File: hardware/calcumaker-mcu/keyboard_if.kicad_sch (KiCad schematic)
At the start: 1 part, among them J5 TO KEYBOARD

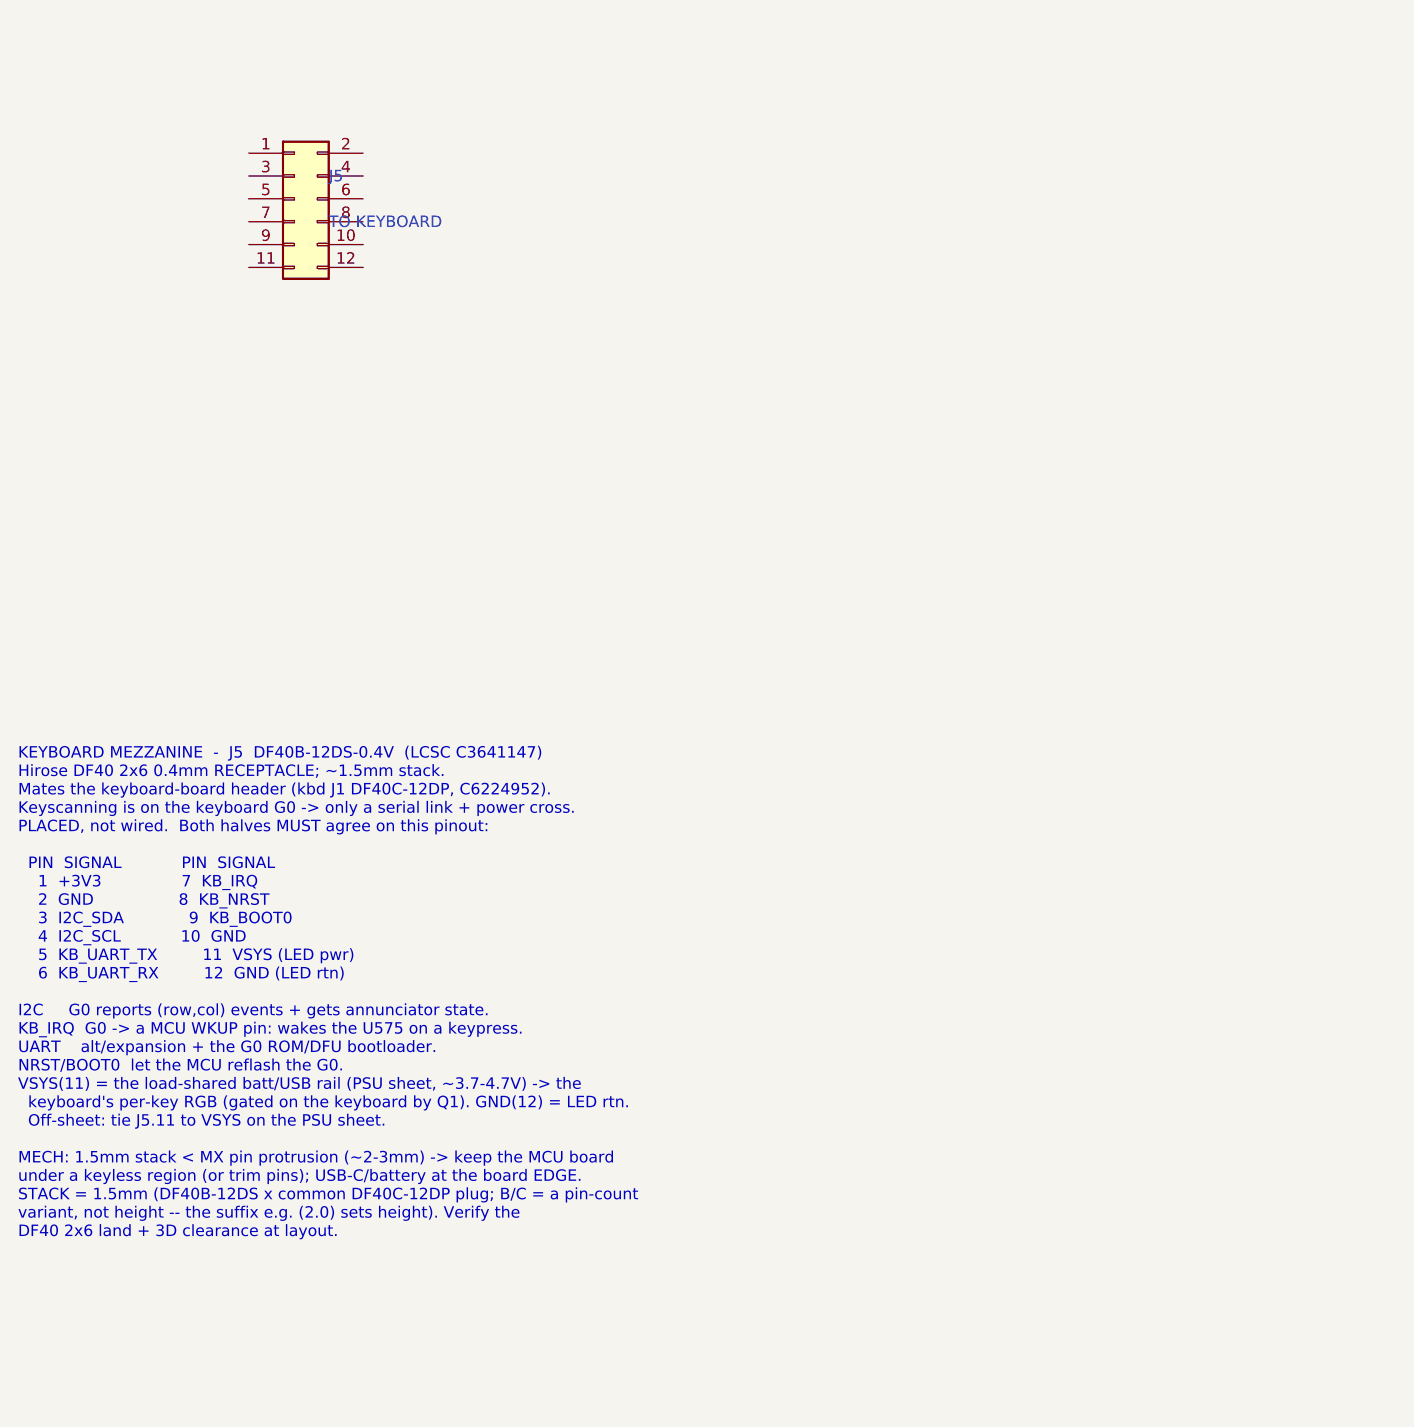
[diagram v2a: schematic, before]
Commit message: hardware: schematic wiring + design/parts updates (WIP)
Pre-existing working-tree changes across the MCU and keyboard boards: wiring
build-out on the mezzanine interfaces (main_if / keyboard_if), MCU/PSU/display/
clock/QSPI sheet edits, per-key row updates, plus DESIGN.md, PARTS.md, and the
two schgen manifests. Committed as-is at the user's request.

Co-Authored-By: Claude Opus 4.8 (1M context) <noreply@anthropic.com>
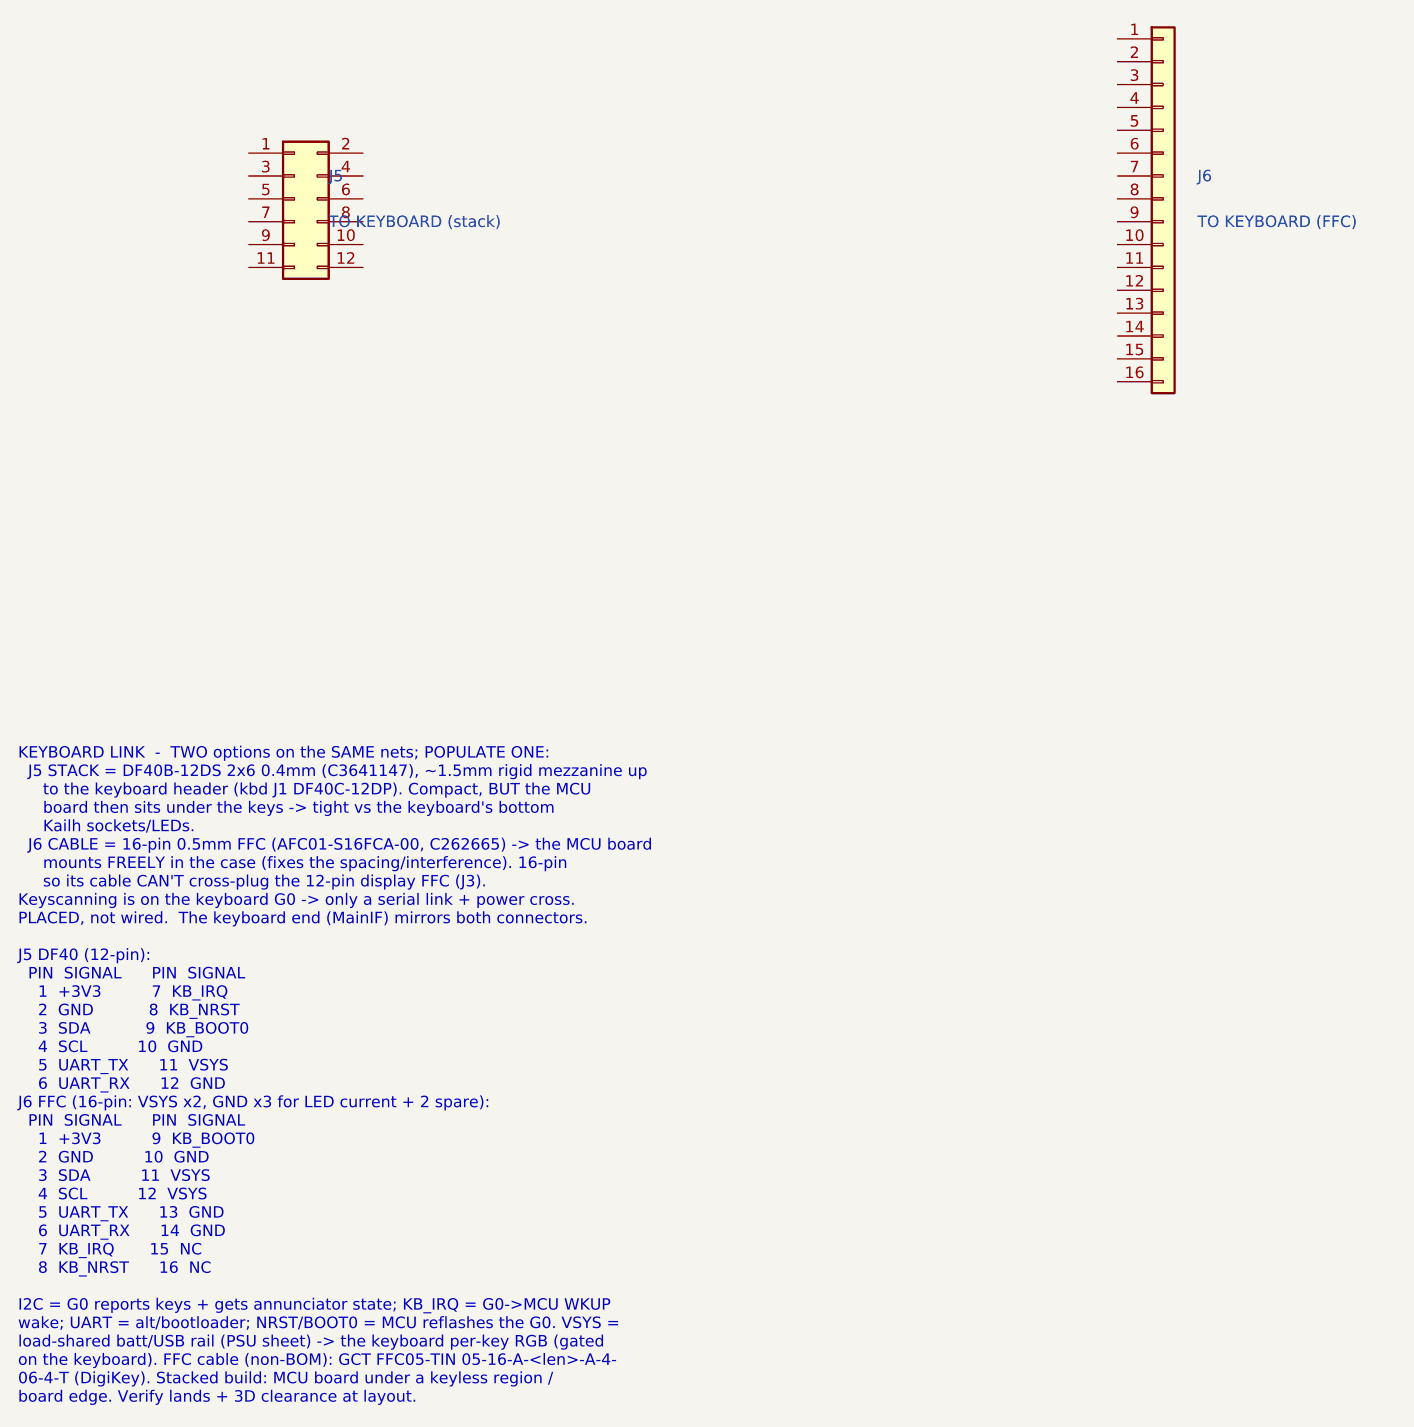
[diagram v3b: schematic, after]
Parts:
- added J6: TO KEYBOARD (FFC), Connector_FFC-FPC:Hirose_FH12-16S-0.5SH_1x16-1MP_P0.50mm_Horizontal, symbol Connector_Generic:Conn_01x16
- J5: value TO KEYBOARD -> TO KEYBOARD (stack)
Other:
- note added: "KEYBOARD LINK - TWO options on the SAME nets; POPULATE ONE: J5 STACK = DF40B-12DS 2x6 0.4mm (C3641147), ~1.5mm rigid mezzanine up to the keyboard header (kbd J1 DF40C-12DP). Compact, BUT the MCU board then sits under the keys -> tight vs the keyboard's bottom Kailh sockets/LEDs. J6 CABLE = 16-pin 0.5mm FFC (AFC01-S16FCA-00, C262665) -> the MCU board mounts FREELY in the case (fixes the spacing/in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"
- note removed: "KEYBOARD MEZZANINE - J5 DF40B-12DS-0.4V (LCSC C3641147) Hirose DF40 2x6 0.4mm RECEPTACLE; ~1.5mm stack. Mates the keyboard-board header (kbd J1 DF40C-12DP, C6224952). Keyscanning is on the keyboard G0 -> only a serial link + power cross. PLACED, not wired. Both halves MUST agree on this pinout: PIN SIGNAL PIN SIGNAL 1 +3V3 7 KB_IRQ 2 GND 8 KB_NRST 3 I2C_SDA 9 KB_BOOT0 4 I2C_SCL 10 GND 5 KB_UART_T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"
- title: Calcumaker 16 — MCU — Keyboard mezzanine (I2C + UART + VSYS to the stacked keyboard) -> Calcumaker 16 — MCU — Keyboard link -- DF40 stack (J5) OR 16-pin FFC cable (J6), populate one
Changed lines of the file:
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@@
 	(paper "A3")
 	(title_block
-		(title "Calcumaker 16 — MCU — Keyboard mezzanine (I2C + UART + VSYS to the stacked keyboard)")
+		(title "Calcumaker 16 — MCU — Keyboard link -- DF40 stack (J5) OR 16-pin FFC cable (J6), populate one")
 		(date "2026-07-06")
 		(rev "0.3")
@@
 			(effects (font (size 1.27 1.27)) (justify left))
 		)
-		(property "Value" "TO KEYBOARD"
+		(property "Value" "TO KEYBOARD (stack)"
 			(at 49.5300 58.4200 0)
 			(effects (font (size 1.27 1.27)) (justify left))
@@
 		)
 	)
-	(text "KEYBOARD MEZZANINE  -  J5  DF40B-12DS-0.4V  (LCSC C3641147)\nHirose DF40 2x6 0.4mm RECEPTACLE; ~1.5mm stack.\nMates the keyboard-board header (kbd J1 DF40C-12DP, C6224952).\nKeyscanning is on the keyboard G0 -> only a serial link + power cross.\nPLACED, not wired.  Both halves MUST agree on this pinout:\n\n  PIN  SIGNAL            PIN  SIGNAL        \n    1  +3V3                7  KB_IRQ        \n    2  GND                 8  KB_NRST       \n    3  I2C_SDA             9  KB_BOOT0      \n    4  I2C_SCL            10  GND           \n    5  KB_UART_TX         11  VSYS (LED pwr)\n    6  KB_UART_RX         12  GND (LED rtn)\n\nI2C     G0 reports (row,col) events + gets annunciator state.\nKB_IRQ  G0 -> a MCU WKUP pin: wakes the U575 on a keypress.\nUART    alt/expansion + the G0 ROM/DFU bootloader.\nNRST/BOOT0  let the MCU reflash the G0.\nVSYS(11) = the load-shared batt/USB rail (PSU sheet, ~3.7-4.7V) -> the\n  keyboard's per-key RGB (gated on the keyboard by Q1). GND(12) = LED rtn.\n  Off-sheet: tie J5.11 to VSYS on the PSU sheet.\n\nMECH: 1.5mm stack < MX pin protrusion (~2-3mm) -> keep the MCU board\nunder a keyless region (or trim pins); USB-C/battery at the board EDGE.\nSTACK = 1.5mm (DF40B-12DS x common DF40C-12DP plug; B/C = a pin-count\nvariant, not height -- the suffix e.g. (2.0) sets height). Verify the\nDF40 2x6 land + 3D clearance at layout."
+	(symbol
+		(lib_id "Connector_Generic:Conn_01x16")
+		(at 142.2400 55.8800 0)
+		(unit 1)
+		(exclude_from_sim no)
+		(in_bom yes)
+		(on_board yes)
+		(dnp no)
+		(property "Reference" "J6"
+			(at 146.0500 53.3400 0)
+			(effects (font (size 1.27 1.27)) (justify left))
+		)
+		(property "Value" "TO KEYBOARD (FFC)"
+			(at 146.0500 58.4200 0)
+			(effects (font (size 1.27 1.27)) (justify left))
+		)
+		(property "Footprint" "Connector_FFC-FPC:Hirose_FH12-16S-0.5SH_1x16-1MP_P0.50mm_Horizontal"
+			(at 142.2400 55.8800 0)
+			(effects (font (size 1.27 1.27))) (hide yes)
+		)
+		(property "Datasheet" "~"
+			(at 142.2400 55.8800 0)
+			(effects (font (size 1.27 1.27))) (hide yes)
+		)
+		(property "LCSC" "C262665"
+			(at 142.2400 55.8800 0)
+			(effects (font (size 1.27 1.27))) (hide yes)
+		)
+		(property "MPN" "AFC01-S16FCA-00"
+			(at 142.2400 55.8800 0)
+			(effects (font (size 1.27 1.27))) (hide yes)
+		)
+		(property "Manufacturer" "JUSHUO"
+			(at 142.2400 55.8800 0)
+			(effects (font (size 1.27 1.27))) (hide yes)
+		)
+		(pin "1")
+		(pin "2")
+		(pin "3")
+		(pin "4")
+		(pin "5")
+		(pin "6")
+		(pin "7")
+		(pin "8")
+		(pin "9")
+		(pin "10")
+		(pin "11")
+		(pin "12")
+		(pin "13")
+		(pin "14")
+		(pin "15")
+		(pin "16")
+		(instances
+			(project "calcumaker-mcu"
+				(path "/ca1c0000-0000-4000-8000-00000000ma01/32aa4625-0e65-45ea-b771-87030b782539"
+					(reference "J6")
+					(unit 1)
+				)
+			)
+		)
+	)
+	(text "KEYBOARD LINK  -  TWO options on the SAME nets; POPULATE ONE:\n  J5 STACK = DF40B-12DS 2x6 0.4mm (C3641147), ~1.5mm rigid mezzanine up\n     to the keyboard header (kbd J1 DF40C-12DP). Compact, BUT the MCU\n     board then sits under the keys -> tight vs the keyboard's bottom\n     Kailh sockets/LEDs.\n  J6 CABLE = 16-pin 0.5mm FFC (AFC01-S16FCA-00, C262665) -> the MCU board\n     mounts FREELY in the case (fixes the spacing/interference). 16-pin\n     so its cable CAN'T cross-plug the 12-pin display FFC (J3).\nKeyscanning is on the keyboard G0 -> only a serial link + power cross.\nPLACED, not wired.  The keyboard end (MainIF) mirrors both connectors.\n\nJ5 DF40 (12-pin):\n  PIN  SIGNAL      PIN  SIGNAL  \n    1  +3V3          7  KB_IRQ  \n    2  GND           8  KB_NRST \n    3  SDA           9  KB_BOOT0\n    4  SCL          10  GND     \n    5  UART_TX      11  VSYS    \n    6  UART_RX      12  GND\nJ6 FFC (16-pin: VSYS x2, GND x3 for LED current + 2 spare):\n  PIN  SIGNAL      PIN  SIGNAL  \n    1  +3V3          9  KB_BOOT0\n    2  GND          10  GND     \n    3  SDA          11  VSYS    \n    4  SCL          12  VSYS    \n    5  UART_TX      13  GND     \n    6  UART_RX      14  GND     \n    7  KB_IRQ       15  NC      \n    8  KB_NRST      16  NC\n\nI2C = G0 reports keys + gets annunciator state; KB_IRQ = G0->MCU WKUP\nwake; UART = alt/bootloader; NRST/BOOT0 = MCU reflashes the G0. VSYS =\nload-shared batt/USB rail (PSU sheet) -> the keyboard per-key RGB (gated\non the keyboard). FFC cable (non-BOM): GCT FFC05-TIN 05-16-A-<len>-A-4-\n06-4-T (DigiKey). Stacked build: MCU board under a keyless region /\nboard edge. Verify lands + 3D clearance at layout."
 		(exclude_from_sim no)
 		(at 15.00 116.88 0)
